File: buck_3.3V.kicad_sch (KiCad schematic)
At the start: 15 parts, among them U1701 TPS566238RQFR

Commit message: Fix schematic ERC errors
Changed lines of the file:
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@@
-	)
-	(junction
-		(at 69.85 62.23)
-		(diameter 0)
-		(color 0 0 0 0)
 	)
 	(junction
@@
 	(wire
 		(pts
-			(xy 69.85 62.23) (xy 71.12 62.23)
-		)
-		(stroke
-			(width 0)
-			(type default)
-		)
-	)
-	(wire
-		(pts
 			(xy 233.68 77.47) (xy 233.68 78.74)
 		)
@@
 	(wire
 		(pts
-			(xy 57.15 62.23) (xy 69.85 62.23)
+			(xy 57.15 62.23) (xy 71.12 62.23)
 		)
 		(stroke
@@
 			)
 		)
-		(property "Sim.Enable" ""
-			(at 233.68 73.66 0)
-			(effects
-				(font
-					(size 1.27 1.27)
-				)
-			)
-		)
 		(pin "1"
 		)
@@
 	)
 	(symbol
-		(lib_id "power:PWR_FLAG")
-		(at 69.85 62.23 0)
-		(unit 1)
-		(exclude_from_sim no)
-		(in_bom yes)
-		(on_board yes)
-		(dnp no)
-		(fields_autoplaced yes)
-		(property "Reference" "#FLG01701"
-			(at 69.85 60.325 0)
-			(effects
-				(font
-					(size 1.27 1.27)
-				)
-				(hide yes)
-			)
-		)
-		(property "Value" "PWR_FLAG"
-			(at 69.85 57.15 0)
-			(effects
-				(font
-					(size 1.27 1.27)
-				)
-			)
-		)
-		(property "Footprint" ""
-			(at 69.85 62.23 0)
-			(effects
-				(font
-					(size 1.27 1.27)
-				)
-				(hide yes)
-			)
-		)
-		(property "Datasheet" "~"
-			(at 69.85 62.23 0)
-			(effects
-				(font
-					(size 1.27 1.27)
-				)
-				(hide yes)
-			)
-		)
-		(property "Description" "Special symbol for telling ERC where power comes from"
-			(at 69.85 62.23 0)
-			(effects
-				(font
-					(size 1.27 1.27)
-				)
-				(hide yes)
-			)
-		)
-		(pin "1"
-		)
-		(instances
-			(project "SH-RPi"
-				(path "/4c14904e-48eb-4243-8cbd-3afad8250b85/00000000-0000-0000-0000-00005ca73f16"
-					(reference "#FLG0201")
-					(unit 1)
-				)
-			)
-			(project "SH-RPi"
-				(path "/abc482bd-3f17-4d35-80db-1da3dcdb5c27/c7bf4e1f-6bd1-4be7-9e56-1bd438bf5d42/531e3be9-7113-42c4-b43f-4c940587f1bb"
-					(reference "#FLG0201")
-					(unit 1)
-				)
-				(path "/abc482bd-3f17-4d35-80db-1da3dcdb5c27/c7bf4e1f-6bd1-4be7-9e56-1bd438bf5d42/e9d5ec1c-aaca-4440-9248-34d6a57da48f"
-					(reference "#FLG01701")
-					(unit 1)
-				)
-			)
-		)
-	)
-	(symbol
 		(lib_id "Device:C")
 		(at 161.29 59.69 270)
@@
 				)
 				(hide yes)
-			)
-		)
-		(property "Sim.Enable" ""
-			(at 161.29 59.69 0)
-			(effects
-				(font
-					(size 1.27 1.27)
-				)
 			)
 		)
@@
 			)
 		)
-		(property "Sim.Enable" ""
-			(at 240.03 78.74 0)
-			(effects
-				(font
-					(size 1.27 1.27)
-				)
-			)
-		)
 		(pin "1"
 		)
@@
 				)
 				(hide yes)
-			)
-		)
-		(property "Sim.Enable" ""
-			(at 222.25 73.66 0)
-			(effects
-				(font
-					(size 1.27 1.27)
-				)
 			)
 		)
@@
 			)
 		)
-		(property "Sim.Enable" ""
-			(at 71.12 71.12 0)
-			(effects
-				(font
-					(size 1.27 1.27)
-				)
-			)
-		)
 		(pin "1"
 		)
@@
 			)
 		)
-		(property "Sim.Enable" ""
-			(at 182.88 80.01 0)
-			(effects
-				(font
-					(size 1.27 1.27)
-				)
-			)
-		)
 		(pin "1"
 		)
@@
 				)
 				(hide yes)
-			)
-		)
-		(property "Sim.Enable" ""
-			(at 222.25 85.09 0)
-			(effects
-				(font
-					(size 1.27 1.27)
-				)
 			)
 		)
@@
 			)
 		)
-		(property "Sim.Enable" ""
-			(at 123.19 72.39 0)
-			(effects
-				(font
-					(size 1.27 1.27)
-				)
-			)
-		)
 		(pin "3"
 		)
@@
 			)
 		)
-		(property "Sim.Enable" ""
-			(at 95.25 82.55 0)
-			(effects
-				(font
-					(size 1.27 1.27)
-				)
-			)
-		)
 		(pin "2"
 		)
@@
 			)
 		)
-		(property "Sim.Enable" ""
-			(at 212.09 73.66 0)
-			(effects
-				(font
-					(size 1.27 1.27)
-				)
-			)
-		)
 		(pin "1"
 		)
@@
 			)
 		)
-		(property "Sim.Enable" ""
-			(at 57.15 71.12 0)
-			(effects
-				(font
-					(size 1.27 1.27)
-				)
-			)
-		)
 		(pin "1"
 		)
@@
 			)
 		)
-		(property "Sim.Enable" ""
-			(at 195.58 76.2 0)
-			(effects
-				(font
-					(size 1.27 1.27)
-				)
-			)
-		)
 		(pin "1"
 		)
@@
 			)
 		)
-		(property "Sim.Enable" ""
-			(at 175.26 67.31 0)
-			(effects
-				(font
-					(size 1.27 1.27)
-				)
-			)
-		)
 		(pin "1"
 		)
@@
 				)
 				(hide yes)
-			)
-		)
-		(property "Sim.Enable" ""
-			(at 154.94 67.31 0)
-			(effects
-				(font
-					(size 1.27 1.27)
-				)
 			)
 		)
@@
 			)
 		)
-		(property "Sim.Enable" ""
-			(at 87.63 91.44 0)
-			(effects
-				(font
-					(size 1.27 1.27)
-				)
-			)
-		)

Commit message: Reannotate components
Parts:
- renumbered C1702 to C1101, C1703 to C1102, C1708 to C1103, C1701 to C1104, C1707 to C1105, C1706 to C1106, C1704 to C1107, C1705 to C1108, L1701 to L1101, R1702 to R1101, R1701 to R1102, R1703 to R1103, TP1701 to TP1101, TP1702 to TP1102, U1701 to U1101
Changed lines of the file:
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@@
 		(on_board yes)
 		(dnp no)
-		(property "Reference" "#PWR01702"
+		(property "Reference" "#PWR01102"
 			(at 71.12 88.9 0)
 			(effects
@@
 			(project "Yellow"
 				(path "/abc482bd-3f17-4d35-80db-1da3dcdb5c27/c7bf4e1f-6bd1-4be7-9e56-1bd438bf5d42/e9d5ec1c-aaca-4440-9248-34d6a57da48f"
-					(reference "#PWR01702")
+					(reference "#PWR01102")
 					(unit 1)
 				)
@@
 		(on_board yes)
 		(dnp no)
-		(property "Reference" "#PWR01705"
+		(property "Reference" "#PWR01106"
 			(at 195.58 91.44 0)
 			(effects
@@
 			(project "HALPI2"
 				(path "/abc482bd-3f17-4d35-80db-1da3dcdb5c27/c7bf4e1f-6bd1-4be7-9e56-1bd438bf5d42/e9d5ec1c-aaca-4440-9248-34d6a57da48f"
-					(reference "#PWR01705")
+					(reference "#PWR01106")
 					(unit 1)
 				)
@@
 		(on_board yes)
 		(dnp no)
-		(property "Reference" "#PWR01704"
+		(property "Reference" "#PWR01107"
 			(at 212.09 91.44 0)
 			(effects
@@
 				)
 				(path "/abc482bd-3f17-4d35-80db-1da3dcdb5c27/c7bf4e1f-6bd1-4be7-9e56-1bd438bf5d42/e9d5ec1c-aaca-4440-9248-34d6a57da48f"
-					(reference "#PWR01704")
+					(reference "#PWR01107")
 					(unit 1)
 				)
@@
 		(on_board yes)
 		(dnp no)
-		(property "Reference" "C1705"
+		(property "Reference" "C1108"
 			(at 236.601 72.4916 0)
 			(effects
@@
 			(project "Yellow"
 				(path "/abc482bd-3f17-4d35-80db-1da3dcdb5c27/c7bf4e1f-6bd1-4be7-9e56-1bd438bf5d42/e9d5ec1c-aaca-4440-9248-34d6a57da48f"
-					(reference "C1705")
+					(reference "C1108")
 					(unit 1)
 				)
@@
 		(on_board yes)
 		(dnp no)
-		(property "Reference" "#PWR01703"
+		(property "Reference" "#PWR01105"
 			(at 182.88 91.44 0)
 			(effects
@@
 			(project "Yellow"
 				(path "/abc482bd-3f17-4d35-80db-1da3dcdb5c27/c7bf4e1f-6bd1-4be7-9e56-1bd438bf5d42/e9d5ec1c-aaca-4440-9248-34d6a57da48f"
-					(reference "#PWR01703")
+					(reference "#PWR01105")
 					(unit 1)
 				)
@@
 		(on_board yes)
 		(dnp no)
-		(property "Reference" "C1701"
+		(property "Reference" "C1104"
 			(at 166.37 55.88 90)
 			(effects
@@
 				)
 				(path "/abc482bd-3f17-4d35-80db-1da3dcdb5c27/c7bf4e1f-6bd1-4be7-9e56-1bd438bf5d42/e9d5ec1c-aaca-4440-9248-34d6a57da48f"
-					(reference "C1701")
+					(reference "C1104")
 					(unit 1)
 				)
@@
 		(on_board yes)
 		(dnp no)
-		(property "Reference" "TP1702"
+		(property "Reference" "TP1102"
 			(at 242.57 80.7719 0)
 			(effects
@@
 			(project "Yellow"
 				(path "/abc482bd-3f17-4d35-80db-1da3dcdb5c27/c7bf4e1f-6bd1-4be7-9e56-1bd438bf5d42/e9d5ec1c-aaca-4440-9248-34d6a57da48f"
-					(reference "TP1702")
+					(reference "TP1102")
 					(unit 1)
 				)
@@
 		(on_board yes)
 		(dnp no)
-		(property "Reference" "R1701"
+		(property "Reference" "R1102"
 			(at 226.06 72.39 0)
 			(effects
@@
 				)
 				(path "/abc482bd-3f17-4d35-80db-1da3dcdb5c27/c7bf4e1f-6bd1-4be7-9e56-1bd438bf5d42/e9d5ec1c-aaca-4440-9248-34d6a57da48f"
-					(reference "R1701")
+					(reference "R1102")
 					(unit 1)
 				)
@@
 		(on_board yes)
 		(dnp no)
-		(property "Reference" "C1703"
+		(property "Reference" "C1102"
 			(at 68.199 69.9516 0)
 			(effects
@@
 			(project "Yellow"
 				(path "/abc482bd-3f17-4d35-80db-1da3dcdb5c27/c7bf4e1f-6bd1-4be7-9e56-1bd438bf5d42/e9d5ec1c-aaca-4440-9248-34d6a57da48f"
-					(reference "C1703")
+					(reference "C1102")
 					(unit 1)
 				)
@@
 		(on_board yes)
 		(dnp no)
-		(property "Reference" "C1707"
+		(property "Reference" "C1105"
 			(at 179.959 78.8416 0)
 			(effects
@@
 			(project "Yellow"
 				(path "/abc482bd-3f17-4d35-80db-1da3dcdb5c27/c7bf4e1f-6bd1-4be7-9e56-1bd438bf5d42/e9d5ec1c-aaca-4440-9248-34d6a57da48f"
-					(reference "C1707")
+					(reference "C1105")
 					(unit 1)
 				)
@@
 		(on_board yes)
 		(dnp no)
-		(property "Reference" "R1703"
+		(property "Reference" "R1103"
 			(at 224.028 83.9216 0)
 			(effects
@@
 				)
 				(path "/abc482bd-3f17-4d35-80db-1da3dcdb5c27/c7bf4e1f-6bd1-4be7-9e56-1bd438bf5d42/e9d5ec1c-aaca-4440-9248-34d6a57da48f"
-					(reference "R1703")
+					(reference "R1103")
 					(unit 1)
 				)
@@
 		(dnp no)
 		(fields_autoplaced yes)
-		(property "Reference" "U1701"
+		(property "Reference" "U1101"
 			(at 123.19 54.61 0)
 			(effects
@@
 				)
 				(path "/abc482bd-3f17-4d35-80db-1da3dcdb5c27/c7bf4e1f-6bd1-4be7-9e56-1bd438bf5d42/e9d5ec1c-aaca-4440-9248-34d6a57da48f"
-					(reference "U1701")
+					(reference "U1101")
 					(unit 1)
 				)
@@
 		(on_board yes)
 		(dnp no)
-		(property "Reference" "R1702"
+		(property "Reference" "R1101"
 			(at 95.25 85.344 90)
 			(effects
@@
 				)
 				(path "/abc482bd-3f17-4d35-80db-1da3dcdb5c27/c7bf4e1f-6bd1-4be7-9e56-1bd438bf5d42/e9d5ec1c-aaca-4440-9248-34d6a57da48f"
-					(reference "R1702")
+					(reference "R1101")
 					(unit 1)
 				)
@@
 		(on_board yes)
 		(dnp no)
-		(property "Reference" "#PWR01701"
+		(property "Reference" "#PWR01101"
 			(at 57.15 88.9 0)
 			(effects
@@
 				)
 				(path "/abc482bd-3f17-4d35-80db-1da3dcdb5c27/c7bf4e1f-6bd1-4be7-9e56-1bd438bf5d42/e9d5ec1c-aaca-4440-9248-34d6a57da48f"
-					(reference "#PWR01701")
+					(reference "#PWR01101")
 					(unit 1)
 				)
@@
 		(on_board yes)
 		(dnp no)
-		(property "Reference" "#PWR01706"
+		(property "Reference" "#PWR01108"
 			(at 222.25 96.52 0)
 			(effects
@@
 				)
 				(path "/abc482bd-3f17-4d35-80db-1da3dcdb5c27/c7bf4e1f-6bd1-4be7-9e56-1bd438bf5d42/e9d5ec1c-aaca-4440-9248-34d6a57da48f"
-					(reference "#PWR01706")
+					(reference "#PWR01108")
 					(unit 1)
 				)
@@
 		(on_board yes)
 		(dnp no)
-		(property "Reference" "C1704"
+		(property "Reference" "C1107"
 			(at 209.169 72.4916 0)
 			(effects
@@
 			(project "HALPI2"
 				(path "/abc482bd-3f17-4d35-80db-1da3dcdb5c27/c7bf4e1f-6bd1-4be7-9e56-1bd438bf5d42/e9d5ec1c-aaca-4440-9248-34d6a57da48f"
-					(reference "C1704")
+					(reference "C1107")
 					(unit 1)
 				)
@@
 		(on_board yes)
 		(dnp no)
-		(property "Reference" "C1702"
+		(property "Reference" "C1101"
 			(at 54.229 69.9516 0)
 			(effects
@@
 				)
 				(path "/abc482bd-3f17-4d35-80db-1da3dcdb5c27/c7bf4e1f-6bd1-4be7-9e56-1bd438bf5d42/e9d5ec1c-aaca-4440-9248-34d6a57da48f"
-					(reference "C1702")
+					(reference "C1101")
 					(unit 1)
 				)
@@
 		(on_board yes)
 		(dnp no)
-		(property "Reference" "#PWR01707"
+		(property "Reference" "#PWR01103"
 			(at 87.63 104.14 0)
 			(effects
@@
 			(project "Yellow"
 				(path "/abc482bd-3f17-4d35-80db-1da3dcdb5c27/c7bf4e1f-6bd1-4be7-9e56-1bd438bf5d42/e9d5ec1c-aaca-4440-9248-34d6a57da48f"
-					(reference "#PWR01707")
+					(reference "#PWR01103")
 					(unit 1)
 				)
@@
 		(on_board yes)
 		(dnp no)
-		(property "Reference" "#PWR01708"
+		(property "Reference" "#PWR01104"
 			(at 123.19 104.14 0)
 			(effects
@@
 			(project "Yellow"
 				(path "/abc482bd-3f17-4d35-80db-1da3dcdb5c27/c7bf4e1f-6bd1-4be7-9e56-1bd438bf5d42/e9d5ec1c-aaca-4440-9248-34d6a57da48f"
-					(reference "#PWR01708")
+					(reference "#PWR01104")
 					(unit 1)
 				)
@@
 		(on_board yes)
 		(dnp no)
-		(property "Reference" "C1706"
+		(property "Reference" "C1106"
 			(at 192.659 75.0316 0)
 			(effects
@@
 			(project "HALPI2"
 				(path "/abc482bd-3f17-4d35-80db-1da3dcdb5c27/c7bf4e1f-6bd1-4be7-9e56-1bd438bf5d42/e9d5ec1c-aaca-4440-9248-34d6a57da48f"
-					(reference "C1706")
+					(reference "C1106")
 					(unit 1)
 				)
@@
 		(dnp no)
 		(fields_autoplaced yes)
-		(property "Reference" "#FLG01702"
+		(property "Reference" "#FLG01101"
 			(at 207.01 65.405 0)
 			(effects
@@
 				)
 				(path "/abc482bd-3f17-4d35-80db-1da3dcdb5c27/c7bf4e1f-6bd1-4be7-9e56-1bd438bf5d42/e9d5ec1c-aaca-4440-9248-34d6a57da48f"
-					(reference "#FLG01702")
+					(reference "#FLG01101")
 					(unit 1)
 				)
@@
 		(on_board yes)
 		(dnp no)
-		(property "Reference" "L1701"
+		(property "Reference" "L1101"
 			(at 175.26 62.484 90)
 			(effects
@@
 				)
 				(path "/abc482bd-3f17-4d35-80db-1da3dcdb5c27/c7bf4e1f-6bd1-4be7-9e56-1bd438bf5d42/e9d5ec1c-aaca-4440-9248-34d6a57da48f"
-					(reference "L1701")
+					(reference "L1101")
 					(unit 1)
 				)
@@
 		(on_board yes)
 		(dnp no)
-		(property "Reference" "TP1701"
+		(property "Reference" "TP1101"
 			(at 157.48 69.3419 0)
 			(effects
@@
 				)
 				(path "/abc482bd-3f17-4d35-80db-1da3dcdb5c27/c7bf4e1f-6bd1-4be7-9e56-1bd438bf5d42/e9d5ec1c-aaca-4440-9248-34d6a57da48f"
-					(reference "TP1701")
+					(reference "TP1101")
 					(unit 1)
 				)
@@
 		(on_board yes)
 		(dnp no)
-		(property "Reference" "C1708"
+		(property "Reference" "C1103"
 			(at 84.709 90.2716 0)
 			(effects
@@
 			(project "Yellow"
 				(path "/abc482bd-3f17-4d35-80db-1da3dcdb5c27/c7bf4e1f-6bd1-4be7-9e56-1bd438bf5d42/e9d5ec1c-aaca-4440-9248-34d6a57da48f"
-					(reference "C1708")
-					(unit 1)
-				)
+					(reference "C1103")
+					(unit 1)
+				)

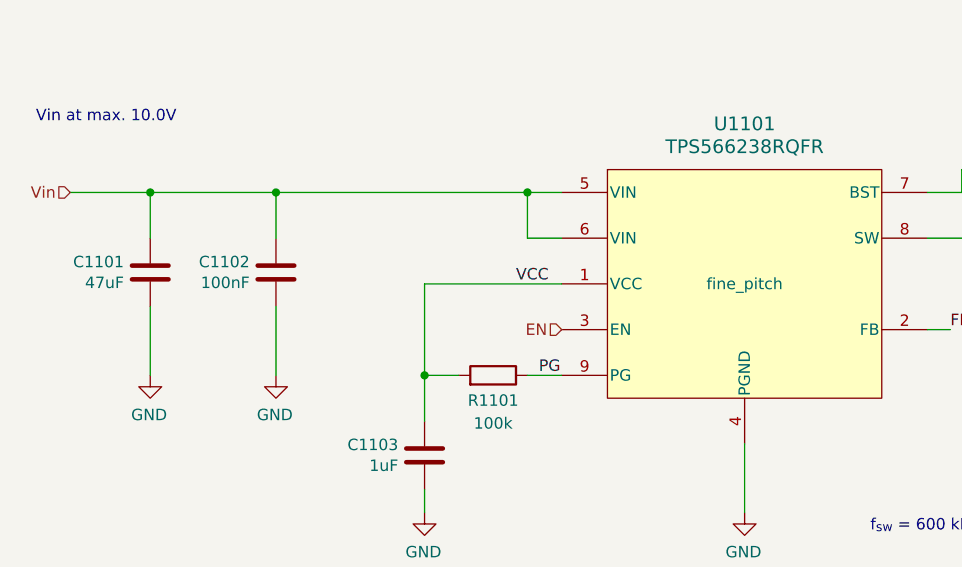
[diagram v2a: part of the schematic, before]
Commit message: Most DRC errors fixed
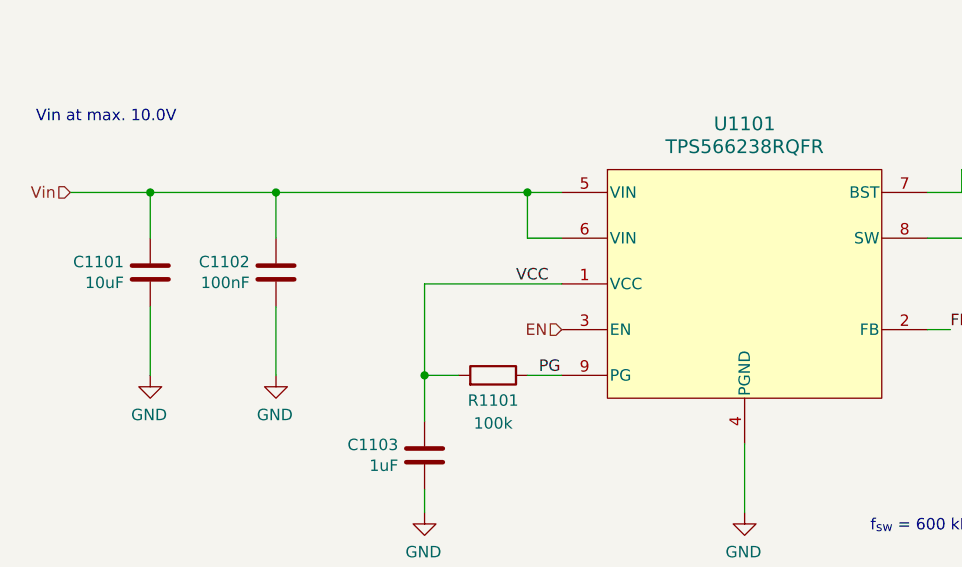
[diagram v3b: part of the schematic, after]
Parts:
- C1101: value 47uF -> 10uF; footprint Capacitor_SMD:C_1210_3225Metric -> Capacitor_SMD:C_1206_3216Metric; LCSC C5440143 -> C13585
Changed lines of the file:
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@@
 					(size 1.27 1.27)
 				)
+				(hide yes)
 			)
 		)
@@
 			)
 		)
-		(property "Value" "47uF"
+		(property "Value" "10uF"
 			(at 54.229 72.263 0)
 			(effects
@@
 			)
 		)
-		(property "Footprint" "Capacitor_SMD:C_1210_3225Metric"
+		(property "Footprint" "Capacitor_SMD:C_1206_3216Metric"
 			(at 56.1848 74.93 0)
 			(effects
@@
 			)
 		)
-		(property "LCSC" "C5440143"
+		(property "LCSC" "C13585"
 			(at 57.15 71.12 0)
 			(effects

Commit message: Silkscreen mostly done
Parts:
- added J1002: 3.3V Header, Connector_PinHeader_2.54mm:PinHeader_2x02_P2.54mm_Vertical, symbol Connector_Generic:Conn_02x02_Odd_Even
- C1102, C1105: value 100nF -> 1uF; LCSC C1525 -> C52923
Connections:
- net GND: now also J1002.1 (Pin_1), J1002.3 (Pin_3)
- net Vout: now also J1002.2 (Pin_2), J1002.4 (Pin_4)

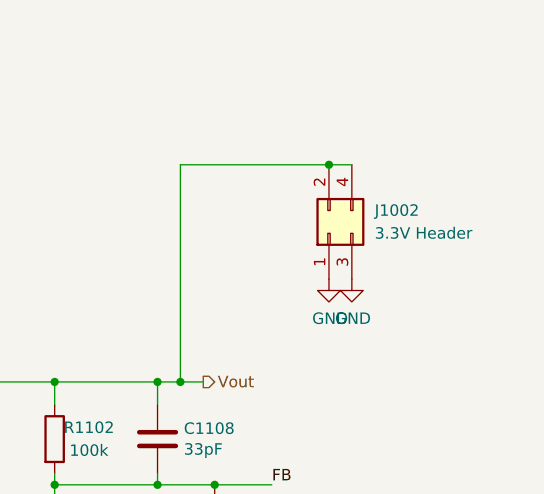
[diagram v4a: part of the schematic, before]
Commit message: Finish the board redesign with SoM on the bottom
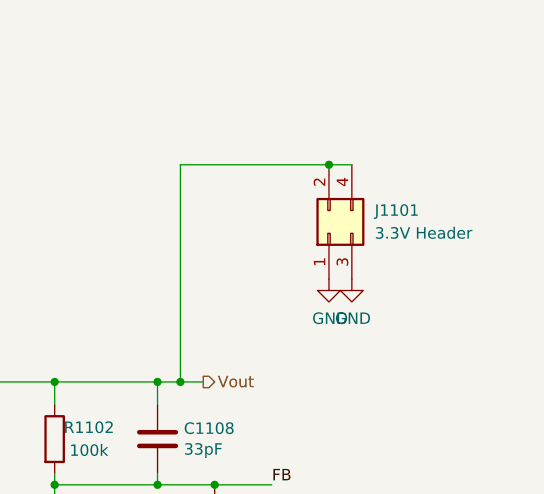
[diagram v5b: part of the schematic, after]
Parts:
- renumbered J1002 to J1101
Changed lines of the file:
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@@
 			)
 		)
-		(property "Description" ""
+		(property "Description" "Unpolarized capacitor"
 			(at 233.68 73.66 0)
 			(effects
@@
 		(dnp no)
 		(fields_autoplaced yes)
-		(property "Reference" "J1002"
+		(property "Reference" "J1101"
 			(at 257.81 48.2599 90)
 			(effects
@@
 			(project "HALPI2"
 				(path "/abc482bd-3f17-4d35-80db-1da3dcdb5c27/c7bf4e1f-6bd1-4be7-9e56-1bd438bf5d42/e9d5ec1c-aaca-4440-9248-34d6a57da48f"
-					(reference "J1002")
+					(reference "J1101")
 					(unit 1)
 				)
@@
 			)
 		)
-		(property "Description" ""
+		(property "Description" "Unpolarized capacitor"
 			(at 161.29 59.69 0)
 			(effects
@@
 			)
 		)
-		(property "Description" ""
+		(property "Description" "test point"
 			(at 240.03 78.74 0)
 			(effects
@@
 			)
 		)
-		(property "Description" ""
+		(property "Description" "Resistor"
 			(at 222.25 73.66 0)
 			(effects
@@
 			)
 		)
-		(property "Description" ""
+		(property "Description" "Unpolarized capacitor"
 			(at 71.12 71.12 0)
 			(effects
@@
 			)
 		)
-		(property "Description" ""
+		(property "Description" "Unpolarized capacitor"
 			(at 182.88 80.01 0)
 			(effects
@@
 			)
 		)
-		(property "Description" ""
+		(property "Description" "Resistor"
 			(at 222.25 85.09 0)
 			(effects
@@
 		(on_board yes)
 		(dnp no)
-		(property "Reference" "#PWR01012"
+		(property "Reference" "#PWR01110"
 			(at 255.27 62.23 0)
 			(effects
@@
 			(project "HALPI2"
 				(path "/abc482bd-3f17-4d35-80db-1da3dcdb5c27/c7bf4e1f-6bd1-4be7-9e56-1bd438bf5d42/e9d5ec1c-aaca-4440-9248-34d6a57da48f"
-					(reference "#PWR01012")
+					(reference "#PWR01110")
 					(unit 1)
 				)
@@
 			)
 		)
-		(property "Description" ""
+		(property "Description" "Unpolarized capacitor"
 			(at 57.15 71.12 0)
 			(effects
@@
 			)
 		)
-		(property "Datasheet" ""
+		(property "Datasheet" "~"
 			(at 195.58 76.2 0)
 			(effects
@@
 			)
 		)
-		(property "Description" ""
+		(property "Description" "Unpolarized capacitor"
 			(at 195.58 76.2 0)
 			(effects
@@
 			)
 		)
-		(property "Description" ""
+		(property "Description" "Inductor"
 			(at 175.26 67.31 0)
 			(effects
@@
 		(on_board yes)
 		(dnp no)
-		(property "Reference" "#PWR01011"
+		(property "Reference" "#PWR01109"
 			(at 252.73 62.23 0)
 			(effects
@@
 			(project "HALPI2"
 				(path "/abc482bd-3f17-4d35-80db-1da3dcdb5c27/c7bf4e1f-6bd1-4be7-9e56-1bd438bf5d42/e9d5ec1c-aaca-4440-9248-34d6a57da48f"
-					(reference "#PWR01011")
+					(reference "#PWR01109")
 					(unit 1)
 				)
@@
 			)
 		)
-		(property "Description" ""
+		(property "Description" "test point"
 			(at 154.94 67.31 0)
 			(effects
@@
 			)
 		)
-		(property "Description" ""
+		(property "Description" "Unpolarized capacitor"
 			(at 87.63 91.44 0)
 			(effects

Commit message: Further refinements
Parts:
- C1107: value 220F/16V -> 220uF/16V
- U1101: value TPS566238RQFR -> TPS566238PRQFR; LCSC C5219353 -> C2876603
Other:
- moved on the sheet: C1106, J1101
